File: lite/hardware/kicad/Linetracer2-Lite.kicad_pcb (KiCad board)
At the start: 2 copper layers, 100 x 100 mm, 30 parts, among them J1 BATTERY (AA x3, XH 2P), J2 I2C (0.96in OLED order), M1 LEFT motor FA-130RA, M2 RIGHT motor FA-130RA, Q1 2SC1815-GR, SW1 START, U1 Raspberry Pi Pico, U2 AE-TC78H653FTG

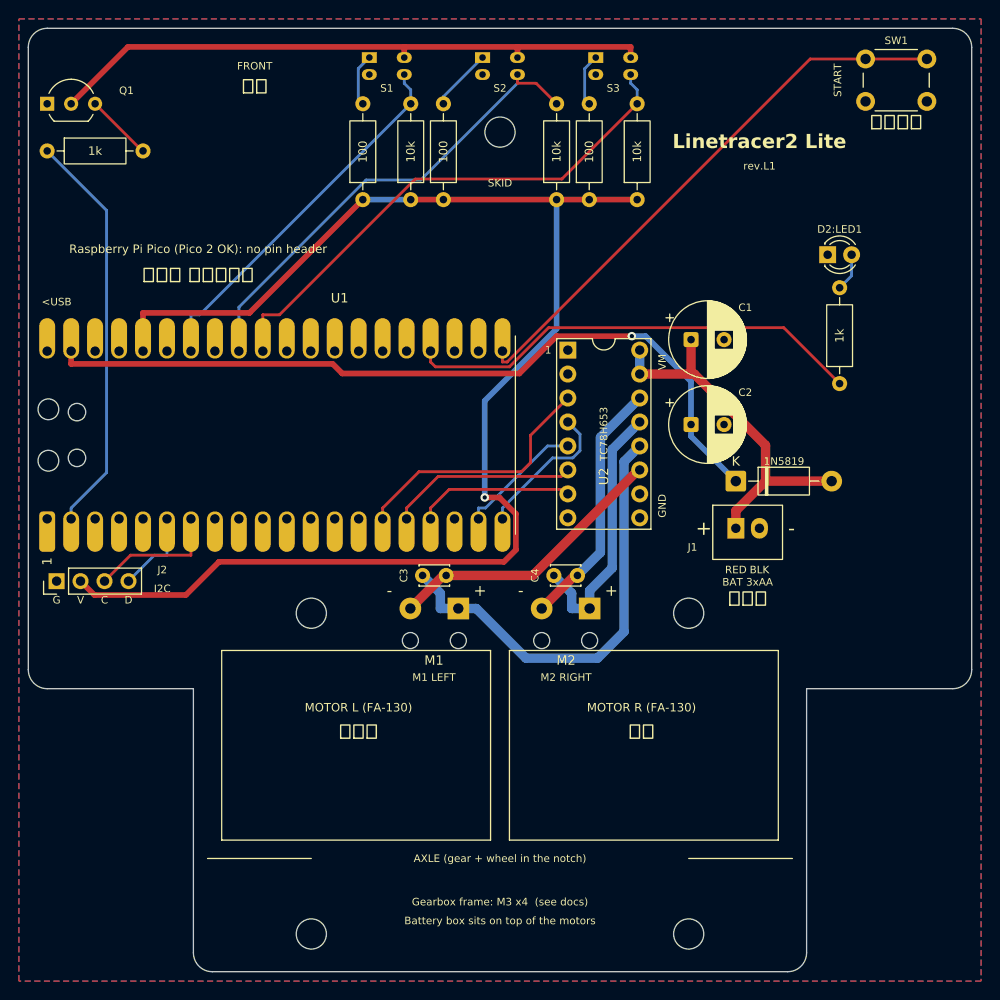
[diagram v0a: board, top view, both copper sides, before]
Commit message: Lite rev.L2: XIAO ESP32C6 と LBR-127HLD に変更、子ども向けに配置・シルクを見直し
- マイコンを Seeed Studio XIAO ESP32C6（秋月 129481）に。ピンヘッダなしで基板にじかにはんだ付け
  （自作フットプリント: 裏のテストパッドの下は銅禁止、USB の足の逃げ穴、アンテナの下は両面銅なし）
- フォトリフレクタを LBR-127HLD（秋月 104500）に。背が 5.6 mm あるのでスキッドを 7.5 mm に
  （skid_clip_h70/h75/h80.stl、ロボットは後ろに 2.9° 傾く。傾きとすき間は scad で計算）
- いらない部品: I2C の穴 J2 を削除。電池電圧の測定はなし（XIAO の ADC 3 本をセンサーで使い切る）
- ピン割り当ては ESP32-C6 の起動時の状態に合わせ、どの瞬間もモーターが回らないようにした
- 基板を 65 x 100 mm の長方形に（面積 -27%、3D プリント部品はそのまま）、抵抗を 6 mm おきに
- シルクは記号だけ（つくる順番の数字、＋、LED の絵、抵抗の 3 本目の色）。説明は手順書 lite/docs/assembly.md
- gen_3d.py の 3D モデルの位置ずれを修正（KiCad は VRML の translation に scale をかけない）
- ERC 0、DRC 0（警告 0・未接続 0）。MicroPython (ESP32_GENERIC_C6) のライブラリとサンプルを移植

Co-Authored-By: Claude Opus 5.5 <noreply@anthropic.com>
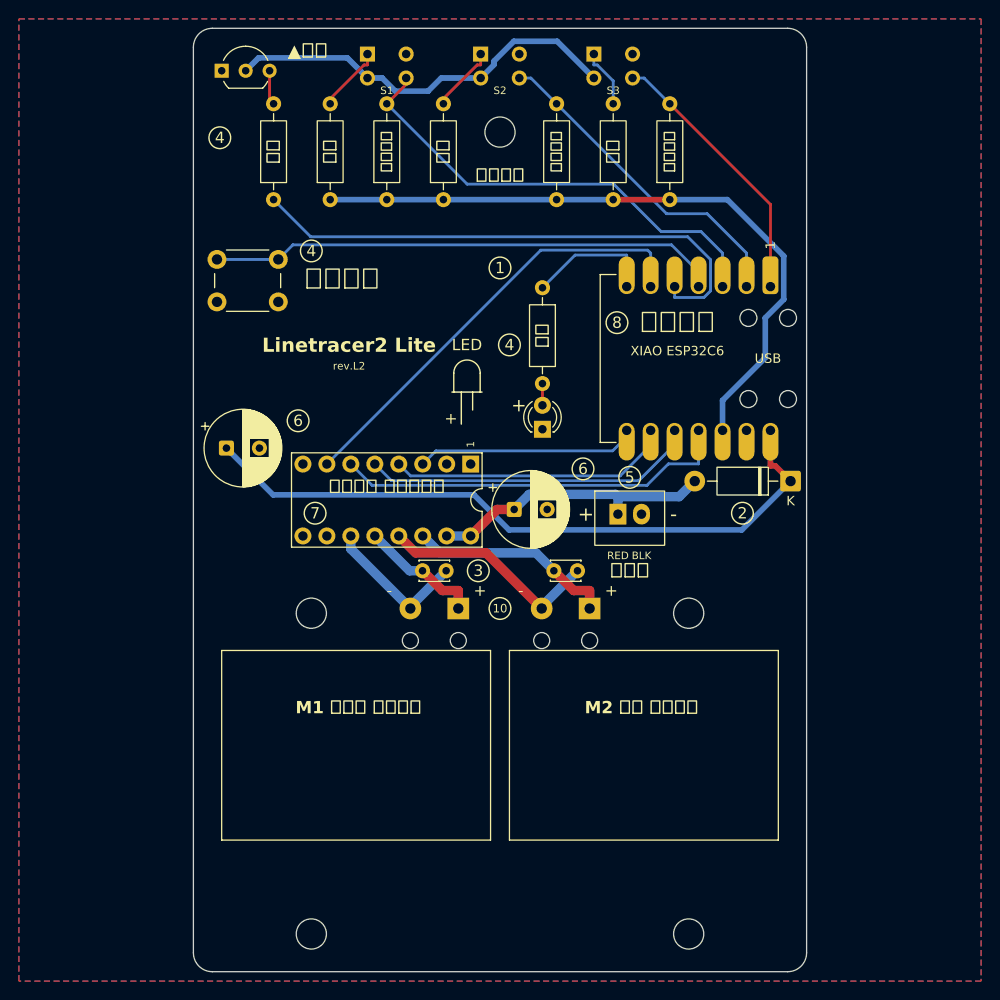
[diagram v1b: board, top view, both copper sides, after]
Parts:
- removed J2: I2C (0.96in OLED order), Connector_PinHeader_2.54mm:PinHeader_1x04_P2.54mm_Vertical
- PS1, PS2, PS3: value LBR-123F -> LBR-127HLD; footprint Linetracer2:LBR-123F -> Linetracer2:LBR-127HLD
- U1: value Raspberry Pi Pico -> XIAO ESP32C6; footprint Linetracer2:RaspberryPi_Pico_DirectSolder -> Linetracer2:XIAO_ESP32C6_DirectSolder
- moved SW1 72.0 mm to (120.0, 74.5)
- moved C2 49.3 mm to (121.0, 94.5)
- moved U1 45.6 mm to (171.1, 85.0), turned to -90 degrees
- moved D2 35.4 mm to (154.5, 92.5), turned to 90 degrees
- moved R8 33.1 mm to (154.5, 77.5), turned to -90 degrees
- moved C1 26.0 mm to (151.5, 101.0)
- moved R7 24.5 mm to (126.0, 68.2), turned to 90 degrees
- moved U2 24.0 mm to (138.0, 100.0), turned to -90 degrees
- moved Q1 18.8 mm to (120.5, 54.5)
- moved J1 12.6 mm to (162.5, 101.5)
- moved D1 5.80 mm to (180.8, 98.0), turned to 180 degrees
- moved R1 3.46 mm to (132.0, 68.2)
- moved R6 3.46 mm to (168.0, 68.2)
- moved R3 2.54 mm to (162.0, 68.2)
- moved R4 2.54 mm to (138.0, 68.2)
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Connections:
- C4 pad 1: /MOT_OUT3 -> /MOT_OUT4
- C4 pad 2: /MOT_OUT4 -> /MOT_OUT3
- M2 pad 1: /MOT_OUT3 -> /MOT_OUT4
- M2 pad 2: /MOT_OUT4 -> /MOT_OUT3
- U1 pad 1: unconnected-(U1-GPIO0-Pad1) -> /SENS3
- U1 pad 10: unconnected-(U1-GPIO7-Pad10) -> /MOT_IN3
- U1 pad 11: unconnected-(U1-GPIO8-Pad11) -> /MOT_IN1
- U1 pad 12: unconnected-(U1-GPIO9-Pad12) -> +3V3
- U1 pad 14: unconnected-(U1-GPIO10-Pad14) -> /VSYS
- U1 pad 2: /SENS_LED_EN -> /SENS2
- U1 pad 3: GND -> /SENS1
- U1 pad 4: unconnected-(U1-GPIO2-Pad4) -> /SW1
- U1 pad 5: unconnected-(U1-GPIO3-Pad5) -> /SENS_LED_EN
- U1 pad 6: /I2C_SDA -> /MOT_IN2
- U1 pad 7: /I2C_SCL -> /LED1
- U1 pad 8: GND -> /MOT_STBY
- U1 pad 9: unconnected-(U1-GPIO6-Pad9) -> /MOT_IN4
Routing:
- net +3V3: track 152.7 -> 71.7 mm, vias 1 -> 0
- net /LED1: track 48.9 -> 13.7 mm
- net /MOT_OUT1: track 47.5 -> 13.1 mm
- net /MOT_IN2: track 16.7 -> 47.4 mm
- net /SENS3: track 56.2 -> 28.9 mm
- net /MOT_IN1: track 19.9 -> 42.3 mm
- net /MOT_IN3: track 13.3 -> 35.6 mm
- net /LED_K: track 65.2 -> 43.0 mm
- net /SENS2: track 50.9 -> 35.3 mm
- net /MOT_IN4: track 15.5 -> 30.2 mm
- net /MOT_OUT2: track 30.4 -> 15.9 mm
- net /SENS_LED_EN: track 43.2 -> 57.5 mm
- net /I2C_SCL: track 14.2 -> 0.00 mm
- net /VSYS: track 83.6 -> 72.1 mm, vias 1 -> 0
- net /SENS1: track 39.8 -> 49.3 mm
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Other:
- board size 100 x 100 mm -> 65 x 100 mm
- board text added: "+"
- board text added: "1"
- board text added: "10"
- board text added: "2"
- board text added: "3"
- board text added: "4"
- board text added: "5"
- board text added: "6"
- board text added: "7"
- board text added: "8"
- board text added: "9"
- board text added: "LED"
- board text added: "M1 ひだり モーター"
- board text added: "M2 みぎ モーター"
- board text added: "USB"
- board text added: "XIAO ESP32C6"
- board text added: "XIAO ESP32C6 + TC78H653FTG + FA-130 x2"
- board text added: "rev.L2"
- board text added: "rev.L2 2026-10 EDTC"
- board text added: "▲まえ"
- board text added: "あか"
- board text added: "こどもむけ ライントレーサー"
- board text added: "だいだい"
- board text added: "ちゃ"
- board text added: "スキッド"
- board text added: "センサー"
- board text added: "マイコン"
- board text added: "モーター ドライバー"
- board text removed: "<USB"
- board text removed: "AXLE (gear + wheel in the notch)"
- board text removed: "BAT 3xAA"
- board text removed: "Battery box sits on top of the motors"
- board text removed: "C"
- board text removed: "D"
- board text removed: "D2:LED1"
- board text removed: "FRONT"
- board text removed: "G"
- board text removed: "Gearbox frame: M3 x4 (see docs)"
- board text removed: "I2C"
- board text removed: "M1 LEFT"
- board text removed: "M2 RIGHT"
- board text removed: "MOTOR L (FA-130)"
- board text removed: "MOTOR R (FA-130)"
- board text removed: "Raspberry Pi Pico (Pico 2 OK): no pin header"
- board text removed: "Raspberry Pi Pico + TC78H653FTG + FA-130 x2"
- board text removed: "SENSOR SIDE: LBR-123F x3 (lens to the floor)"
- board text removed: "SKID"
- board text removed: "START"
- board text removed: "V"
- board text removed: "rev.L1"
- board text removed: "rev.L1 2026-10 EDTC"
- board text removed: "じかに はんだづけ"
- board text removed: "ひだり"
- board text removed: "まえ"
- board text removed: "みぎ"
- board text removed: "センサーはこちらの面に付ける"
- board text removed: "子ども向けライントレーサー教材"

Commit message: Lite rev.L3 基板: XIAO をピンヘッダで、ブザー追加、配線を手で引き直し、シルクを改良
- XIAO ESP32C6 を 2 列 x 7 ピンのスルーホール（ピンヘッダ）に。直付け用フットプリントは削除
- 圧電スピーカー BZ1（PKM13EPYH4000-A0）＋ R9 100 Ω を赤 LED と同じ D6 に
- 自動配線をやめ、lite/scripts/layout_lite.py に配置と配線を書いた（縦・横・45°、直角は面取り、
  バスで並べる、表で交差なし、ビア 0）。route_lite.py で KiCad に入れる。build_pcb.py は Lite では手配線
- 線が交差しないようにピンを 2 か所入れかえ（D3⇄D4、D8⇄D10）
- シルク: 抵抗の絵と ①ちゃ ②だいだい ③あか、つくる順番 ①〜⑮、電解コンデンサの黒い半分に白い −、
  センサーの ● / ○ / ◤
- 配置の確認用の絵: lite/scripts/preview_layout.py（KiCad なしで動く）
- DRC 0・未接続 0・回路図との不一致 0、ERC 0

Co-Authored-By: Claude Opus 5.5 <noreply@anthropic.com>
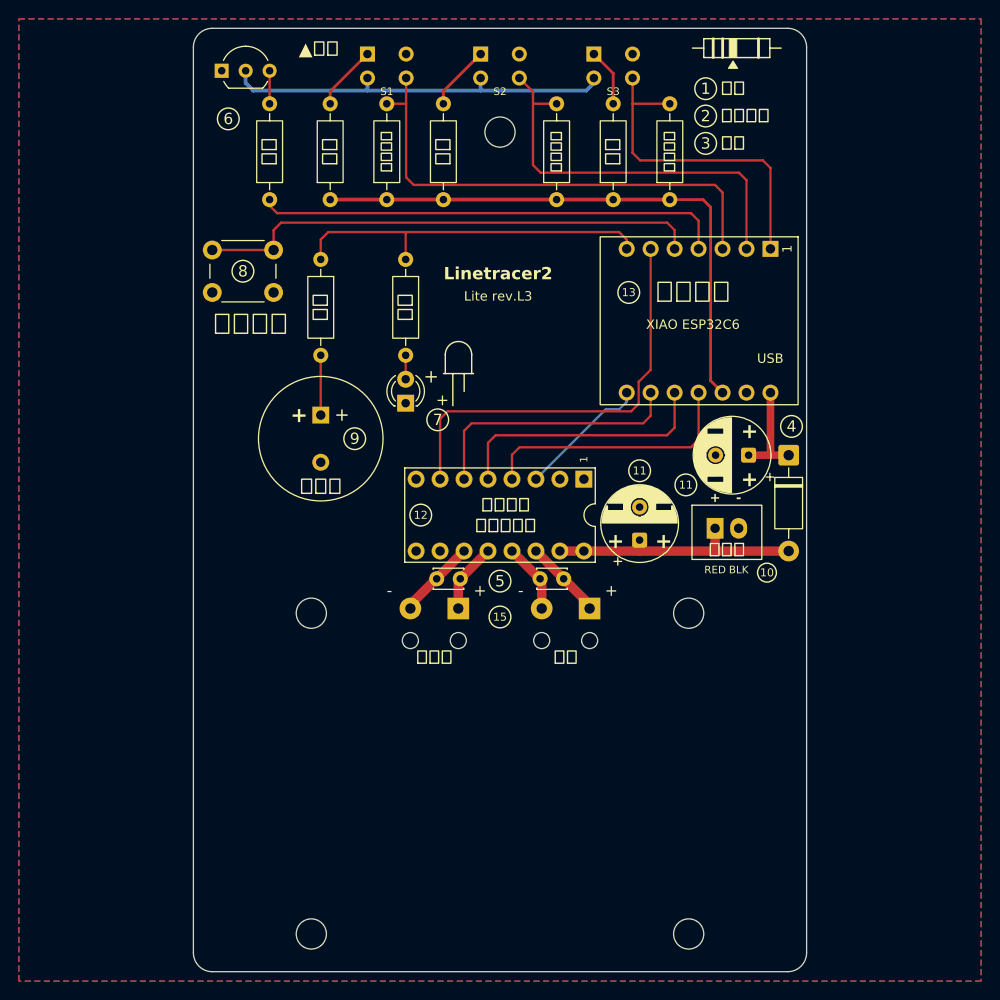
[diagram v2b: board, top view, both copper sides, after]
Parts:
- added BZ1: piezo 13mm, Linetracer2:Buzzer_PKM13_P5.0, F.Cu at (131.0, 91.0)
- added R9: 100, Resistor_THT:R_Axial_DIN0207_L6.3mm_D2.5mm_P10.16mm_Horizontal, F.Cu at (131.0, 74.5)
- U1: footprint Linetracer2:XIAO_ESP32C6_DirectSolder -> Linetracer2:XIAO_ESP32C6_Header
- moved C2 55.4 mm to (176.3, 95.2), turned to 180 degrees
- moved R8 14.8 mm to (140.0, 74.5)
- moved D2 14.8 mm to (140.0, 89.7)
- moved C1 13.7 mm to (164.8, 104.2), turned to 90 degrees
- moved U2 12.1 mm to (150.0, 101.6)
- moved J1 10.4 mm to (172.8, 103.0)
- moved C3 4.09 mm to (145.8, 108.3), turned to 180 degrees
- moved U1 4.00 mm to (171.1, 81.0)
- moved D1 2.76 mm to (180.6, 95.2), turned to -90 degrees
- moved C4 1.34 mm to (156.8, 108.3), turned to 180 degrees
- moved SW1 1.12 mm to (119.5, 73.5)
- moved R7 0.42 mm to (125.6, 68.2)
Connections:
- U1 pad 11: /MOT_IN1 -> /MOT_IN4
- U1 pad 4: /SW1 -> /SENS_LED_EN
- U1 pad 5: /SENS_LED_EN -> /SW1
- U1 pad 9: /MOT_IN4 -> /MOT_IN1
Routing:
- net /VSYS: track 72.1 -> 10.9 mm
- net /LED1: track 13.7 -> 39.1 mm
- net /MOT_OUT3: track 23.9 -> 7.39 mm
- net /MOT_IN1: track 42.3 -> 28.0 mm
- net /MOT_OUT4: track 22.0 -> 8.45 mm
- net +3V3: track 71.7 -> 60.8 mm
- net /MOT_STBY: track 23.5 -> 14.0 mm
- net /SENS_LED_EN: track 57.5 -> 49.8 mm
- net /MOT_IN3: track 35.6 -> 28.0 mm
- net /SENS2: track 35.3 -> 42.9 mm
- net /MOT_OUT2: track 15.9 -> 8.45 mm
- net /SENS3: track 28.9 -> 35.7 mm
- net Net-(BZ1-+): track 0.00 -> 6.34 mm
- net /MOT_OUT1: track 13.1 -> 7.39 mm
- net /SENS1: track 49.3 -> 52.8 mm
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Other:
- board text added: "-"
- board text added: "11"
- board text added: "12"
- board text added: "13"
- board text added: "14"
- board text added: "15"
- board text added: "Linetracer2"
- board text added: "Lite rev.L3"
- board text added: "rev.L3 2026-10 EDTC"
- board text added: "ひだり"
- board text added: "みぎ"
- board text added: "キャスター"
- board text added: "ドライバー"
- board text added: "ブザー"
- board text added: "モーター"
- board text removed: "LED"
- board text removed: "M1 ひだり モーター"
- board text removed: "M2 みぎ モーター"
- board text removed: "rev.L2"
- board text removed: "rev.L2 2026-10 EDTC"
- board text removed: "スキッド"
- board text removed: "モーター ドライバー"

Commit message: 子ども向けレビューの反映: 向きの印・手順・安全・ソフト、手順ごとの絵
- シルク: モータードライバーに「VM」、電解コンデンサの丸の外にも − / ＋（付けたあとも確かめられる）、
  KiCad の小さい ＋ を消した、LED の − を四角い穴に、⑭ うら、2 けたの番号を大きく
- つくる順番: ⑪ モータードライバー → ⑫ XIAO → ⑬ 470 µF（いちばん背が高いので最後）
- J1 のパッドを 1.5 mm 幅に（＋ と − の間 0.7 → 1.0 mm）
- 手順書: こども用（ひらがな）と先生用の列、手順ごとの絵（lite/scripts/step_images.py）、電気を入れる前の
  先生チェック（向き・テスター・D1）、電池は最後まで入れない、保護めがね、うごかしかたカード
- ソフト: キャリブレーションの前に 1 秒待つ、判定 CAL_MIN_SPAN 4000、長押し 1.5 秒＋カチッ、
  音量 robot.volume としずかモード、Ctrl-C でもモーターを止める（motors.off）

Co-Authored-By: Claude Opus 5.5 <noreply@anthropic.com>
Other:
- board text added: "VM"
- board text added: "うら"

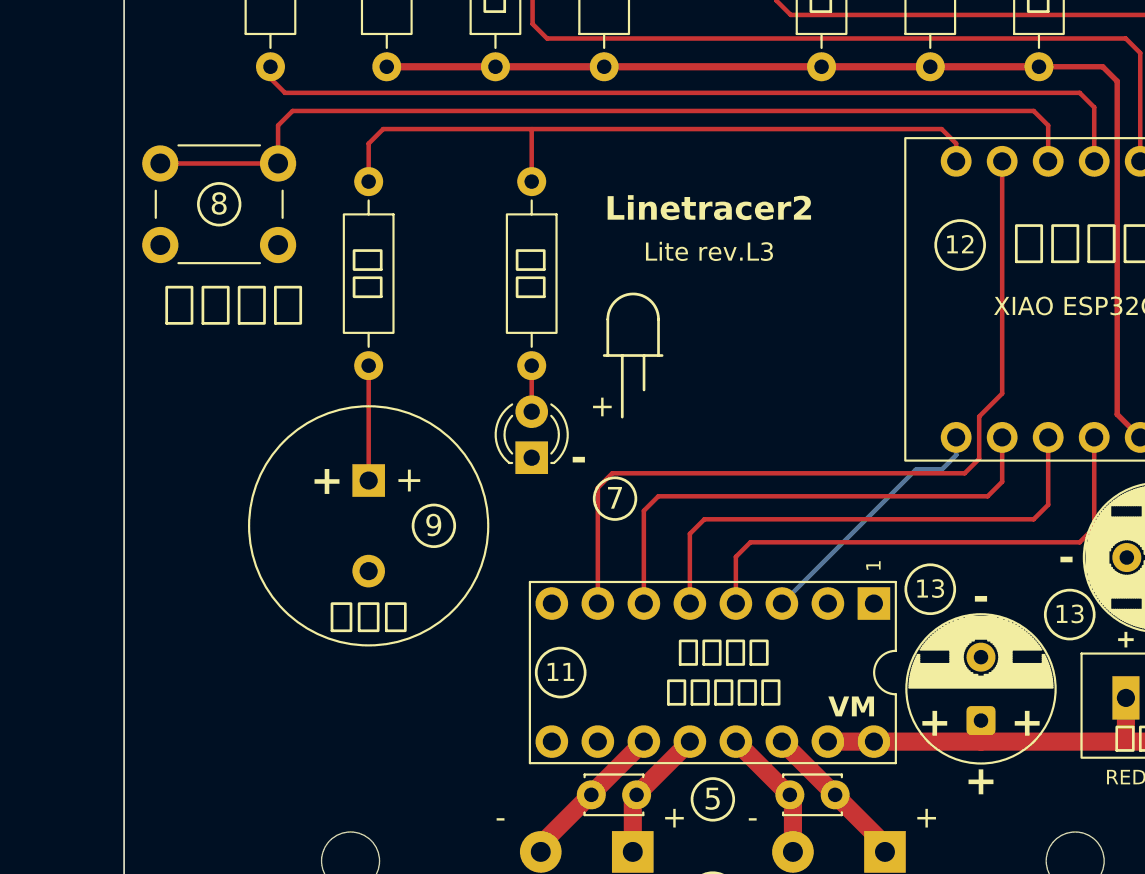
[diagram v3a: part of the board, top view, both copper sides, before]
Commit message: ブザーを START ボタンのピン（D4）へ移し（R10 を追加）、ギヤボックスをデータシートで見直した
- ブザー: D6（赤 LED と共用）→ D4（START と共用）。ボタンは R10 1kΩ、圧電は R9 100Ω を通す。
  圧電は直流を通さないのでボタンはふつうに読め、押したままでも鳴る。LED は D6 を単独で使える。
  ソフトの beep() は D4 を一瞬 PWM の出力にしてから入力に戻す
- 基板: R10 を足して配置・配線をやり直し（DRC / ERC 0、ビア 0、配線 625 mm）。手順 ③ は あか 3 本
- ギヤボックス: FA-130 の公差（軸の出っぱり 9.5 ±0.5、ガタ 0.4）で軸の先とピニオンが外かべに当たりうる
  → 外かべに逃げ穴 φ6.5、壁を前へ 3 mm（check_shaft_wall、逃げ穴なしで検出できることも確認）。
  モーターはツメの摩擦だけで内側へずれうる → デッキの下にリブ（0.3 mm の面取り付き）。
  ピニオンを歯の形（8T）で描く
- 図: hardware/mechanical/gearbox_review.png（scripts/gearbox_figure.py）
- 出力を作り直した（Gerber・BOM・PDF・基板の 3D・手順の絵・ロボット全体の STL / GLB。干渉チェックは全部空）

Co-Authored-By: Claude Opus 5.5 <noreply@anthropic.com>
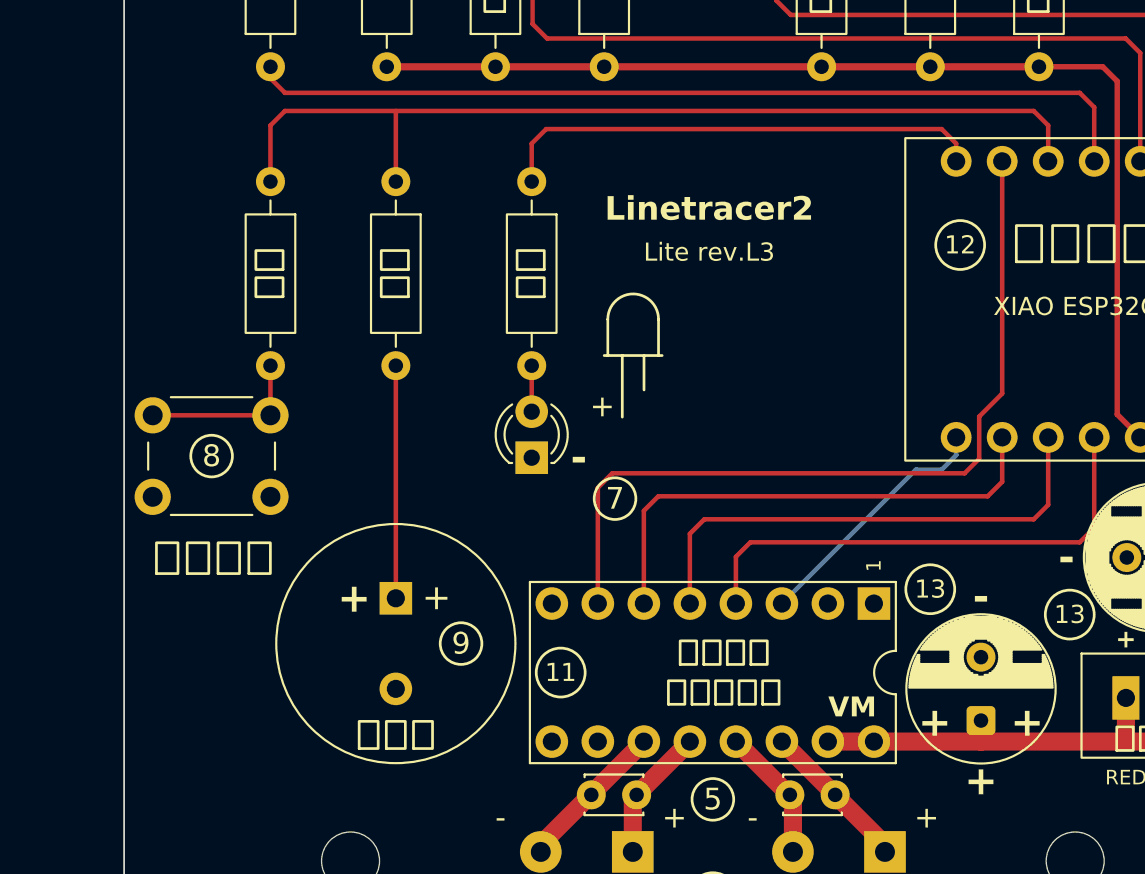
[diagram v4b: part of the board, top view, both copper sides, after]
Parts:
- added R10: 1k, Resistor_THT:R_Axial_DIN0207_L6.3mm_D2.5mm_P10.16mm_Horizontal, F.Cu at (125.6, 74.5)
- moved SW1 13.9 mm to (119.1, 87.4)
- moved BZ1 6.67 mm to (132.5, 97.5)
- moved R9 1.50 mm to (132.5, 74.5)
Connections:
- R9 pad 1: /LED1 -> /SW1
- SW1 pad 1: /SW1 -> /BTN
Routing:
- net /LED1: track 39.1 -> 27.2 mm
- net /BTN: track 0.00 -> 9.24 mm
- net Net-(BZ1-+): track 6.34 -> 12.8 mm
- net /SW1: track 53.8 -> 52.6 mm

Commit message: Lite: 赤 LED をフルカラー LED PL9823 ×5 に、部品表を更新
- D2〜D6 = PL9823-F5（秋月 108411、NeoPixel 型）を D6 の 1 本の信号線でつなぐ。前 3 こ・うしろ 2 こを
  3.5 mm ずつずらして並べ、走っている間は線の位置を 5 だんかいで光らせる
- 電源は VSYS（裏の 1 本、2 列の間に横線）、C5 0.1 µF。赤 LED と R8 をなくした
- 足 1.27 mm の 4 本足は穴を前後に互いちがいに、● の点で GND（いちばん長い足）の穴を示す
- 背が高いので、つくる順番を ⑦ ボタン ⑧ ブザー ⑨ でんち ⑩ ドライバー ⑪ XIAO ⑫ フルカラー LED に付け直した
- DRC / ERC 0、ビア 0、干渉チェックはすべて空。手順の絵・3D・Gerber を作り直した
- ソフト: robot.led（色・fill・bar・count、value は今までどおり）、状態を色で表示、サンプル 07_rgb_led.py
- 部品表 lite/docs/bom.md を更新（1 台 約 ¥2,730、10 台分の秋月 ¥25,440）

Co-Authored-By: Claude Opus 5.5 <noreply@anthropic.com>
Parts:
- removed R8: 1k, Resistor_THT:R_Axial_DIN0207_L6.3mm_D2.5mm_P10.16mm_Horizontal
- added C5: 0.1uF, Capacitor_THT:C_Disc_D3.0mm_W2.0mm_P2.50mm, F.Cu at (136.0, 81.3)
- added D3: PL9823, Linetracer2:LED_PL9823_5mm, F.Cu at (146.0, 77.0)
- added D4: PL9823, Linetracer2:LED_PL9823_5mm, F.Cu at (153.0, 77.0)
- added D5: PL9823, Linetracer2:LED_PL9823_5mm, F.Cu at (149.5, 84.0)
- added D6: PL9823, Linetracer2:LED_PL9823_5mm, F.Cu at (142.5, 84.0)
- D2: value LED red -> PL9823; footprint LED_THT:LED_D3.0mm -> Linetracer2:LED_PL9823_5mm
- moved D2 12.8 mm to (139.0, 77.0), turned to 0 degrees
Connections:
- U1 pad 7: /LED1 -> /RGB_DIN
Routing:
- net /VSYS: track 10.9 -> 95.6 mm
- net /RGB_DIN: track 0.00 -> 31.7 mm
- net /LED1: track 27.2 -> 0.00 mm
- net Net-(D4-DO): track 0.00 -> 8.45 mm
- net Net-(D3-DO): track 0.00 -> 3.94 mm
- net Net-(D5-DO): track 0.00 -> 3.94 mm
- net Net-(D2-DO): track 2.54 -> 3.94 mm
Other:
- board text added: "Linetracer2 Lite rev.L3"
- board text removed: "Linetracer2"
- board text removed: "Lite rev.L3"
